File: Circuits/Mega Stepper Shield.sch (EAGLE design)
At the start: 21 parts, among them T1 2N2222

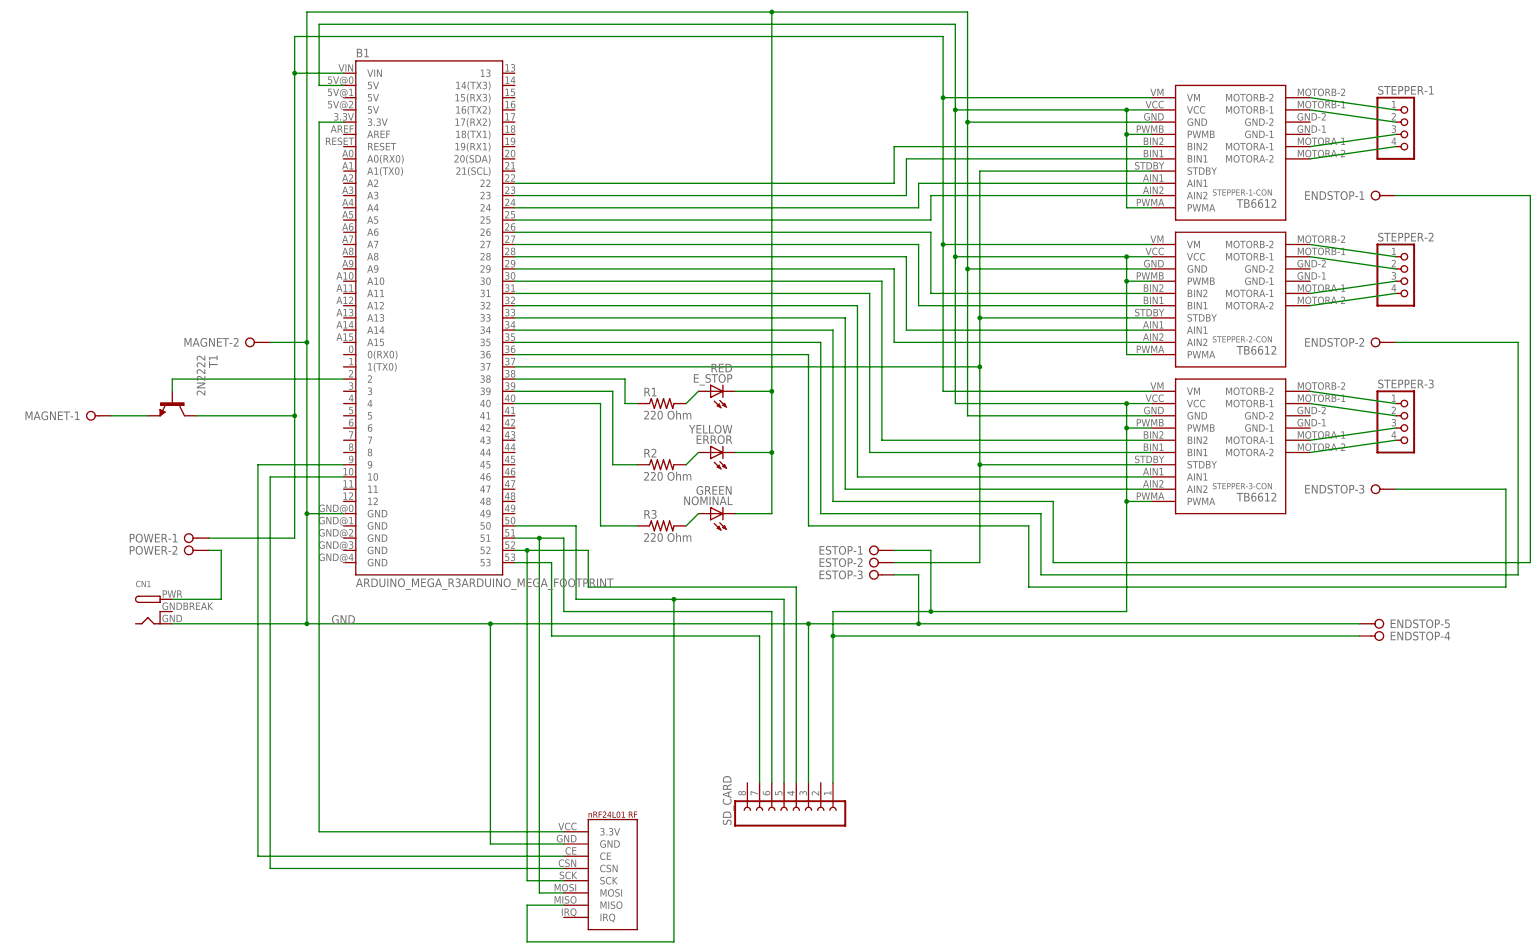
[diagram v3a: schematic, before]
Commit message: Update Board
Added SPI Bus, changed symbol for SD Card Breakout, changed board layout
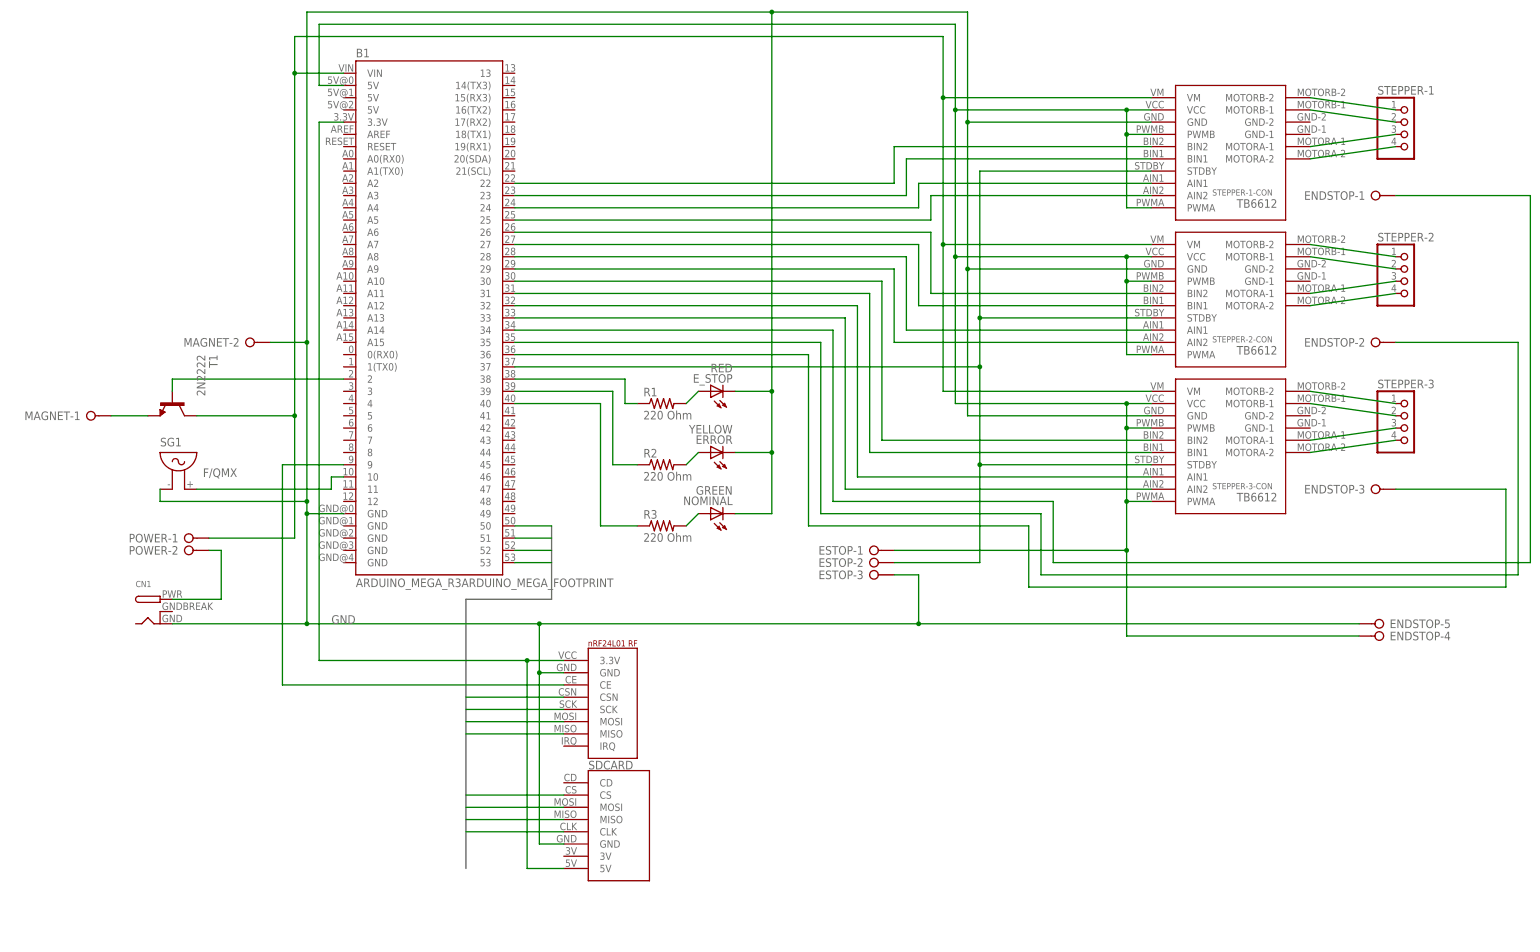
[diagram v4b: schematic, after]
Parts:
- removed SD_CARD: (no value), con-lsta:FE08-1
- added SDCARD: MICRO_SD_BREAKOUT, SparkFun-Boards-Expanded:MICRO_SD_BREAKOUT
- added SG1: F/QMX, buzzer:F/QMX
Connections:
- removed net N$28: B1.52, SD_CARD.4, U$1.SCK
- removed net N$29: B1.50, SD_CARD.5, U$1.MISO
- removed net N$30: B1.51, SD_CARD.6, U$1.MOSI
- removed net N$31: B1.53, SD_CARD.7
- removed net N$35: B1.10, U$1.CSN
- new net CLK: B1.52, SDCARD.CLK, U$1.SCK
- new net CS: B1.53, SDCARD.CS, U$1.CSN
- new net MISO: B1.50, SDCARD.MISO, U$1.MISO
- new net MOSI: B1.51, SDCARD.MOSI, U$1.MOSI
- new net N$2: B1.10, SG1.2
- net 3.3V: now also SDCARD.5V
- net 5V: no longer SD_CARD.1
- net GND: now also SDCARD.GND, SG1.1; no longer SD_CARD.3

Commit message: Update Circuit and include electrical mount
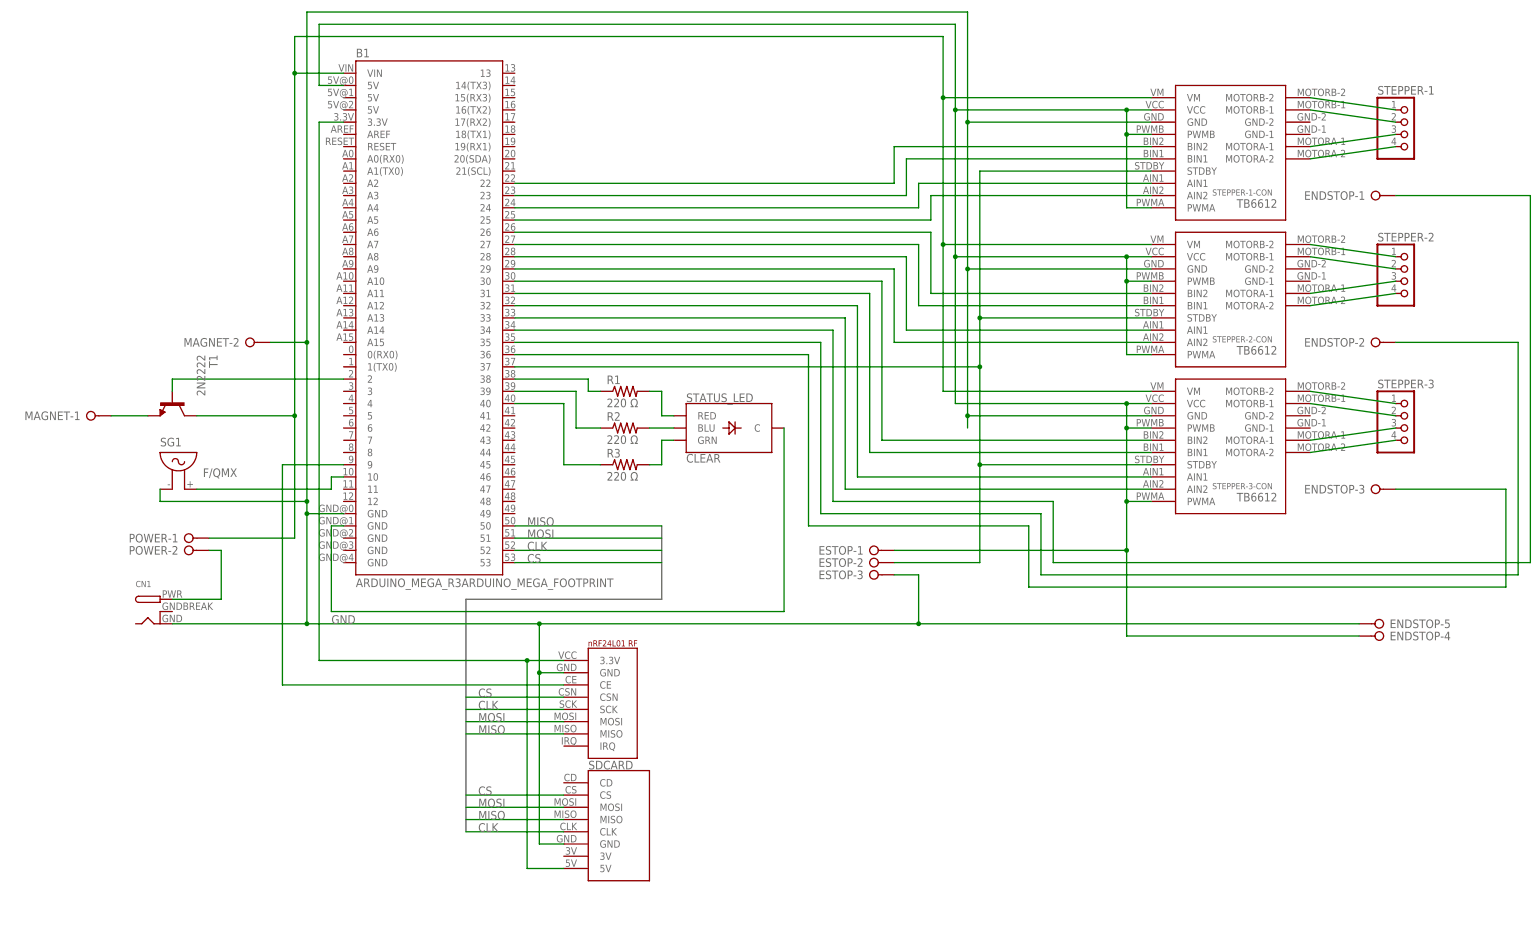
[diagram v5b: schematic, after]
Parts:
- removed ERROR: YELLOW, adafruit:LED5MM
- removed E_STOP: RED, adafruit:LED5MM
- removed NOMINAL: GREEN, adafruit:LED5MM
- added STATUS_LED: CLEAR, SparkFun-LED:LED-RGB-CCCLEAR
- R1, R2, R3: value 220 Ohm -> 220 Ω
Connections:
- removed net N$33: NOMINAL.A, R3.2
- removed net N$36: ERROR.A, R2.2
- removed net N$37: E_STOP.A, R1.2
- new net N$28: R3.2, STATUS_LED.GRN
- new net N$29: R2.2, STATUS_LED.BLU
- new net N$30: R1.2, STATUS_LED.RED
- new net N$31: B1.GND@1, STATUS_LED.C
- net GND: no longer ERROR.C, E_STOP.C, NOMINAL.C
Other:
- moved on the sheet: R1, R2, R3
